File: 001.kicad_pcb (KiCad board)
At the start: 2 copper layers, 63.5 x 109.2 mm, 36 parts, among them CN11 02-XH-A, CN12 02-XH-A, CN21 02-XH-A, CN22 02-XH-A, J11 RJ45, J12 RJ45, J21 J21-FROM-PSE, J22 J22-PD-LAN, K11 JQC-3FF, K21 JQC-3FF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

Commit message: PCB変更とRJ45コネクタのFP作り
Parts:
- moved RV11 207.1 mm to (177.3, -757.9)
- moved FL11 205.2 mm to (196.6, -757.2)
- moved R11 140.2 mm to (169.7, -774.5)
- moved C11 92.1 mm to (64.1, -732.2)
- moved CN11 92.1 mm to (102.5, -742.4)
- moved D11 92.1 mm to (61.9, -749.5)
- moved D12 92.1 mm to (60.2, -726.0)
- moved D13 92.1 mm to (64.9, -716.0)
- moved F11 92.1 mm to (62.3, -740.7)
- moved R12 92.1 mm to (62.7, -711.5)
- moved U11 92.1 mm to (93.7, -714.2)
- moved CN12 92.1 mm to (96.1, -729.2)
- moved J12 51.4 mm to (217.9, -746.5), turned to 270 degrees
- moved J11 49.0 mm to (217.4, -770.6), turned to 270 degrees
- moved K11 20.7 mm to (200.4, -741.7), turned to 270 degrees

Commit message: もうちょっとRJ45コネクタは大変更
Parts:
- D23: value PWR LED -> LED
- J11, J12: footprint Connector_RJ:RJ45_Amphenol_RJHSE5380 -> HOLLY:RJ45_Neltron_7810-8P8C
- J21: value J21-FROM-PSE -> RJ45; footprint Connector_RJ:RJ45_Amphenol_RJHSE5380 -> HOLLY:RJ45_Neltron_7810-8P8C
- J22: value J22-PD-LAN -> RJ45; footprint Connector_RJ:RJ45_Amphenol_RJHSE5380 -> HOLLY:RJ45_Neltron_7810-8P8C
- moved J21 2.52 mm to (165.3, -817.6), turned to 270 degrees
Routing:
- net Net-(J22-Pad5): track 0.00 -> 30.5 mm
- net /PD1: track 30.5 -> 0.00 mm
- net /PD_PWR: track 39.9 -> 65.3 mm
- net /PD2: track 25.3 -> 0.00 mm

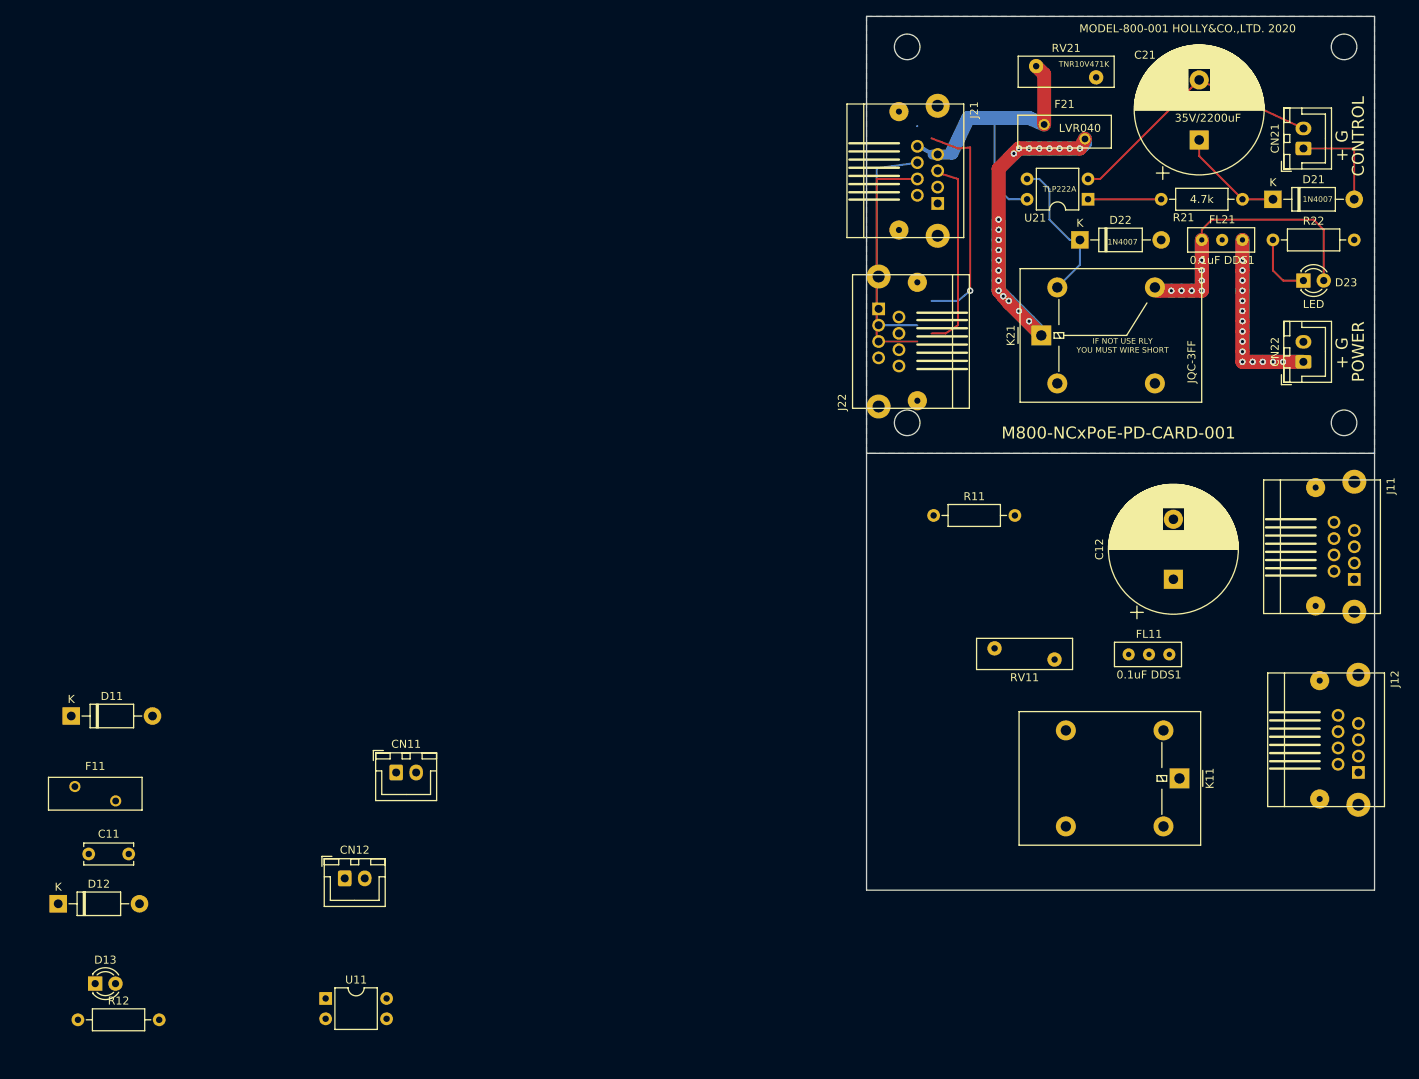
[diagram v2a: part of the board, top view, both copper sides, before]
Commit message: RJ45 SOCKETを組み直し
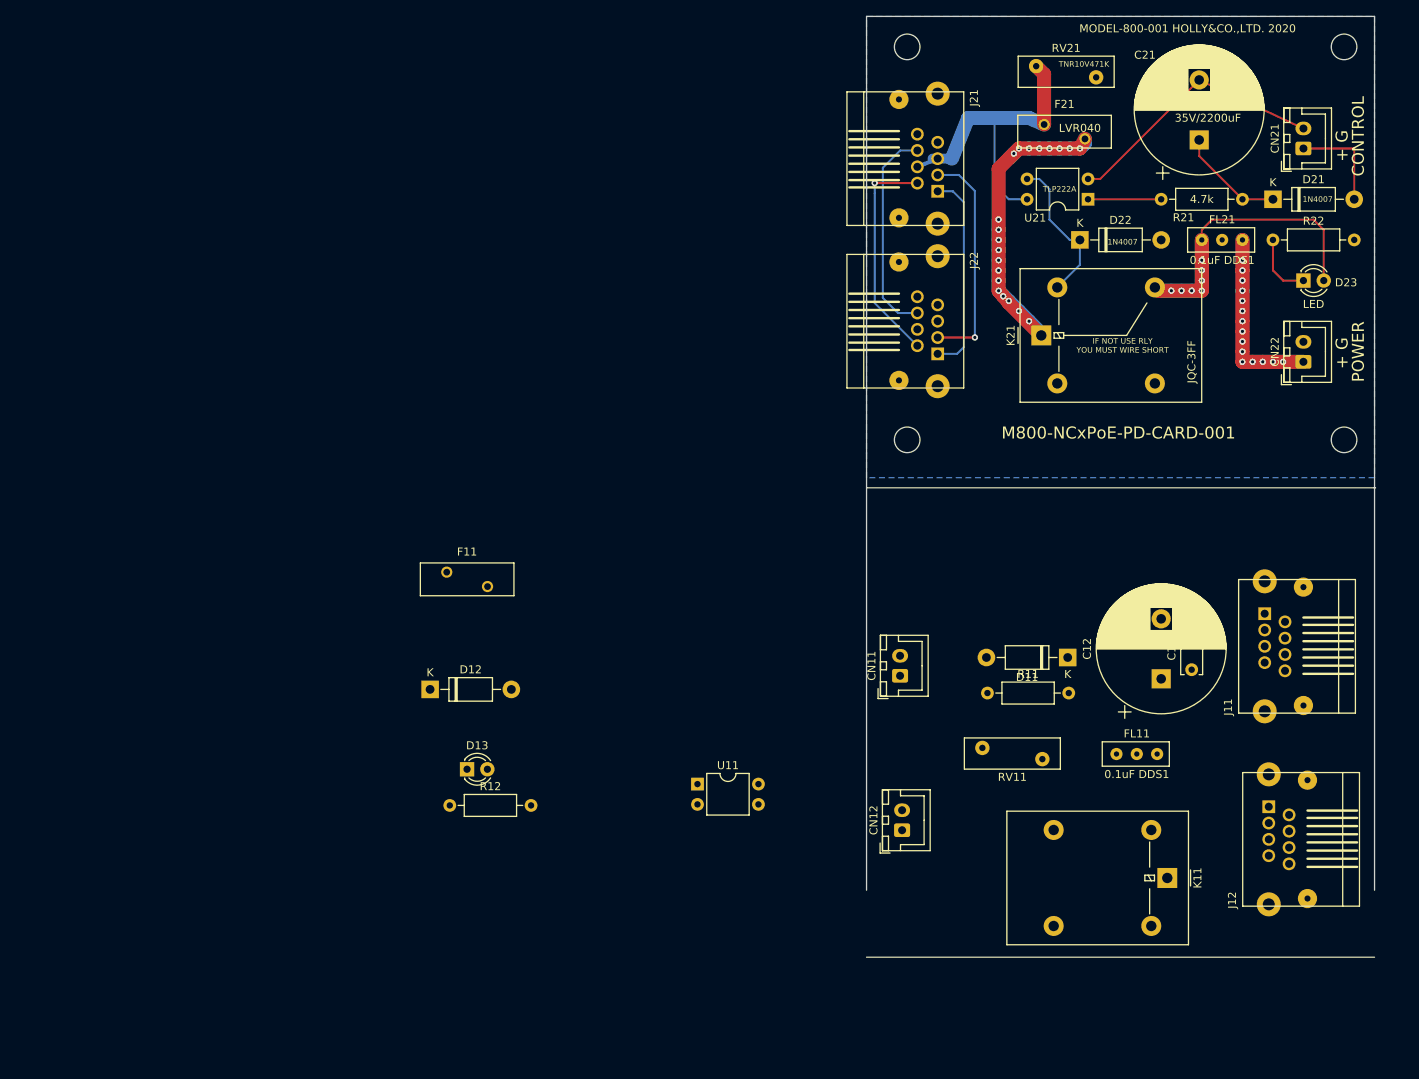
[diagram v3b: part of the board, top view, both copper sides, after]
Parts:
- moved C11 139.8 mm to (201.9, -755.3), turned to 90 degrees
- moved D11 124.8 mm to (186.4, -756.8), turned to 180 degrees
- moved CN12 69.9 mm to (165.7, -735.2), turned to 90 degrees
- moved CN11 64.1 mm to (165.5, -754.5), turned to 90 degrees
- moved F11 53.7 mm to (108.8, -767.5)
- moved D12 53.7 mm to (106.7, -752.8)
- moved D13 53.7 mm to (111.4, -742.8)
- moved U11 53.7 mm to (140.2, -741.0)
- moved R12 53.7 mm to (109.2, -738.3)
- moved R11 23.2 mm to (176.4, -752.3)
- moved C12 12.5 mm to (198.1, -754.1)
- moved FL11 12.5 mm to (195.1, -744.7)
- moved J12 12.5 mm to (216.4, -734.1), turned to 90 degrees
- moved RV11 12.5 mm to (175.8, -745.5)
- moved J11 12.5 mm to (215.9, -758.2), turned to 90 degrees
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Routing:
- net Net-(J22-Pad5): track 30.5 -> 0.00 mm
- net /PD2: track 0.00 -> 27.8 mm, vias 0 -> 1
- net /PD1: track 0.00 -> 25.6 mm
- net /PD_PWR: track 65.3 -> 40.7 mm
- net /PD4: track 28.3 -> 26.6 mm, vias 1 -> 0
- net /PD3: track 29.8 -> 28.4 mm, vias 0 -> 1
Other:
- board size 63.5 x 109.2 mm -> 63.6 x 117.6 mm

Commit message: 更に小型化
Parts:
- removed EC?: DSS1, M800-NCxPoE:DSS1
- removed the REF** at (221.0, -833.1)
- removed the REF** at (221.0, -784.0)
- removed the REF** at (166.4, -784.0)
- removed the REF** at (166.4, -833.1)
- added REF**: MountingHole_3.2mm_M3, MountingHole:MountingHole_3.2mm_M3, F.Cu at (229.9, 61.0)
- added REF**: MountingHole_3.2mm_M3, MountingHole:MountingHole_3.2mm_M3, F.Cu at (229.9, 110.5)
- added REF**: MountingHole_3.2mm_M3, MountingHole:MountingHole_3.2mm_M3, F.Cu at (181.6, 110.5)
- added REF**: MountingHole_3.2mm_M3, MountingHole:MountingHole_3.2mm_M3, F.Cu at (181.6, 61.0)
- moved FL21 905.6 mm to (219.7, 96.5), turned to 270 degrees
- moved D21 904.3 mm to (219.7, 90.2), turned to 90 degrees
- moved R21 904.2 mm to (212.1, 90.2), turned to 90 degrees
- moved D22 899.4 mm to (207.0, 90.2), turned to 90 degrees
- moved D23 899.2 mm to (226.1, 95.2)
- moved CN22 899.2 mm to (219.7, 105.4), turned to 0 degrees
- moved K21 898.7 mm to (195.6, 101.6)
- moved CN21 895.4 mm to (227.3, 74.9)
- moved J22 894.2 mm to (180.6, 95.2)
- moved J21 894.2 mm to (180.6, 74.9)
- moved F21 894.2 mm to (195.6, 70.7)
- moved RV21 894.2 mm to (201.9, 64.8)
- moved C21 894.2 mm to (214.6, 72.6)
- moved U21 894.2 mm to (200.7, 80.0), turned to 270 degrees
- moved R22 889.1 mm to (226.1, 80.0), turned to 270 degrees
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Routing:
- net Net-(CN22-Pad1): track 45.7 -> 6.35 mm, vias 15 -> 0
- net /PD_PWR: track 40.7 -> 69.2 mm, vias 0 -> 11
- net Net-(C21-Pad2): track 33.4 -> 47.4 mm
- net Net-(D23-Pad2): track 48.7 -> 36.4 mm, vias 7 -> 5
- net Net-(C21-Pad1): track 13.5 -> 25.2 mm
- net Net-(D23-Pad1): track 8.15 -> 17.9 mm
- net Net-(F21-Pad2): track 63.1 -> 72.5 mm, vias 20 -> 29
- net Net-(R21-Pad2): track 9.14 -> 15.0 mm
- net /PD1: track 25.6 -> 24.3 mm
- net /PD3: track 28.4 -> 27.3 mm
- net Net-(CN21-Pad1): track 12.7 -> 12.0 mm
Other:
- board size 63.6 x 117.6 mm -> 162.6 x 57.2 mm

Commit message: 一応完成、これからガーバー
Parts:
- added REF**: MountingHole_3.2mm_M3, MountingHole:MountingHole_3.2mm_M3, F.Cu at (122.1, 111.8)
- added REF**: MountingHole_3.2mm_M3, MountingHole:MountingHole_3.2mm_M3, F.Cu at (73.8, 111.8)
- added REF**: MountingHole_3.2mm_M3, MountingHole:MountingHole_3.2mm_M3, F.Cu at (73.8, 63.8)
- added REF**: MountingHole_3.2mm_M3, MountingHole:MountingHole_3.2mm_M3, F.Cu at (122.1, 63.8)
- moved R12 35.9 mm to (76.2, 83.2), turned to 270 degrees
- moved F11 34.4 mm to (106.0, 78.1), turned to 180 degrees
- moved U11 27.1 mm to (106.0, 83.2), turned to 270 degrees
- moved D12 26.8 mm to (99.7, 92.7), turned to 90 degrees
- moved RV11 26.8 mm to (108.0, 71.1), turned to 180 degrees
- moved FL11 25.0 mm to (83.8, 99.7), turned to 90 degrees
- moved D11 23.1 mm to (81.3, 92.7), turned to 90 degrees
- moved C12 21.2 mm to (88.3, 75.6)
- moved C11 17.4 mm to (101.6, 64.8), turned to 180 degrees
- moved D13 14.5 mm to (73.7, 99.1)
- moved CN12 13.3 mm to (83.8, 109.2), turned to 180 degrees
- moved J11 10.3 mm to (121.3, 77.5)
- moved J12 9.86 mm to (121.3, 97.8)
- moved R11 9.16 mm to (95.9, 84.5), turned to 180 degrees
- moved K21 2.79 mm to (192.8, 101.6)
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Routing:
- net /PSE_PWR: track 0.00 -> 83.6 mm
- net Net-(C11-Pad2): track 0.00 -> 54.3 mm
- net Net-(F11-Pad2): track 0.00 -> 46.8 mm
- net Net-(C11-Pad1): track 0.00 -> 38.2 mm
- net Net-(F11-Pad1): track 0.00 -> 30.7 mm
- net /PSEBUS2: track 0.00 -> 26.9 mm
- net /PSEBUS4: track 0.00 -> 24.4 mm
- net /PSEBUS1: track 0.00 -> 23.1 mm
- net /PSEBUS3: track 0.00 -> 23.1 mm
- net Net-(D12-Pad1): track 0.00 -> 17.1 mm
- net Net-(R11-Pad1): track 0.00 -> 13.4 mm
- net Net-(CN22-Pad1): track 6.35 -> 16.3 mm
- net Net-(CN11-Pad1): track 0.00 -> 7.82 mm
- net Net-(CN12-Pad1): track 0.00 -> 6.98 mm
- net /PSE_GND: track 0.00 -> 6.66 mm, vias 0 -> 2
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- added copper zone on B.Cu, net /PSE_GND
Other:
- board size 162.6 x 57.2 mm -> 162.4 x 58.7 mm
- board text added: "G +"
- board text added: "M800-NCxPoE-PSE-CARD-001"

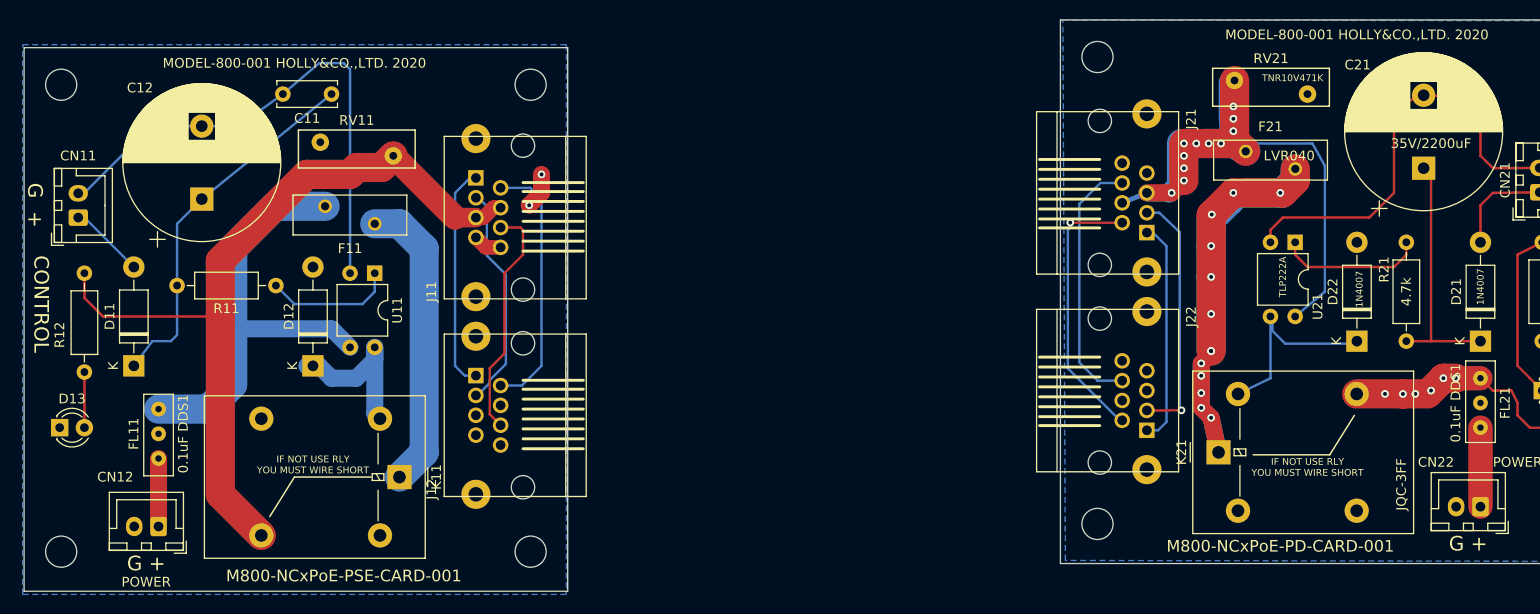
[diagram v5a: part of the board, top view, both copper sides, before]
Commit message: PSEとPDを別図面にした
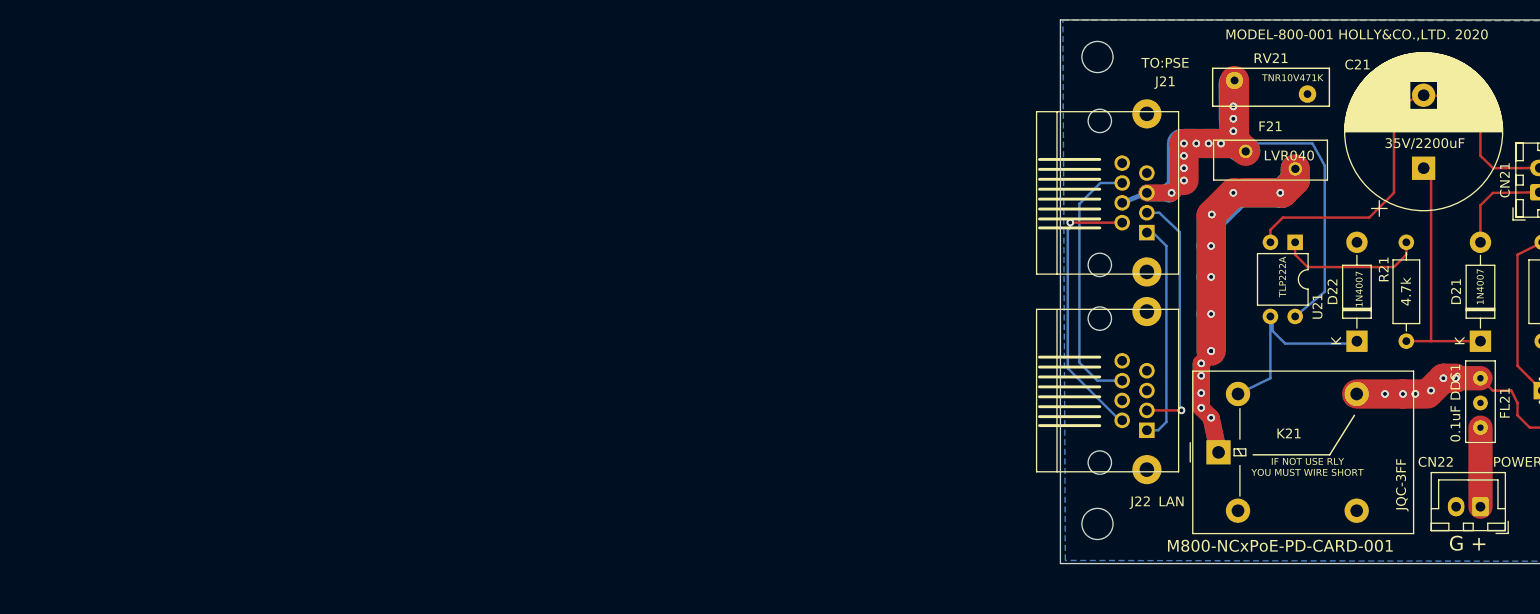
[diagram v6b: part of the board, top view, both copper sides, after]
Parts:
- removed C11: 35V/10uF, Capacitor_THT:C_Disc_D6.0mm_W2.5mm_P5.00mm
- removed C12: 35V/2200uF, Capacitor_THT:CP_Radial_D16.0mm_P7.50mm
- removed CN11, CN12: 02-XH-A, Connector_JST:JST_XH_B2B-XH-A_1x02_P2.50mm_Vertical
- removed D11, D12: 1N4007, Diode_THT:D_DO-41_SOD81_P10.16mm_Horizontal
- removed D13: LED, LED_THT:LED_D3.0mm
- removed F11: LVR040, Fuse:Fuse_BelFuse_0ZRE0033FF_L11.4mm_W3.8mm
- removed FL11: 0.1uF DDS1, HOLLY:DSS1
- removed J11, J12: RJ45, HOLLY:RJ45_Neltron_7810-8P8C
- removed K11: JQC-3FF, Relay_THT:Relay_SPDT_Omron-G5LE-1
- removed R11: 4.7k, Resistor_THT:R_Axial_DIN0207_L6.3mm_D2.5mm_P10.16mm_Horizontal
- removed R12: R_US, Resistor_THT:R_Axial_DIN0207_L6.3mm_D2.5mm_P10.16mm_Horizontal
- removed the REF** at (122.1, 111.8)
- removed the REF** at (73.8, 111.8)
- removed the REF** at (73.8, 63.8)
- removed the REF** at (122.1, 63.8)
- removed RV11: TNR10V471K, Varistor:RV_Disc_D12mm_W3.9mm_P7.5mm
- removed U11: TLP222A, Package_DIP:DIP-4_W7.62mm
- added ?: , , F.Cu at (-13.3, -2.54)
- added ?: , , F.Cu at (22.9, -6.99)
- added ? (x2): , , F.Cu at (85.1, 73.0)
- added ?: , , F.Cu at (87.0, 73.0)
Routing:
- net /PSE_PWR: track 83.6 -> 0.00 mm
- net Net-(C11-Pad2): track 54.3 -> 0.00 mm
- net Net-(F11-Pad2): track 46.8 -> 0.00 mm
- net Net-(C11-Pad1): track 38.2 -> 0.00 mm
- net Net-(F11-Pad1): track 30.7 -> 0.00 mm
- net /PSEBUS2: track 26.9 -> 0.00 mm
- net /PSEBUS4: track 24.4 -> 0.00 mm
- net /PSEBUS1: track 23.1 -> 0.00 mm
- net /PSEBUS3: track 23.1 -> 0.00 mm
- net Net-(D12-Pad1): track 17.1 -> 0.00 mm
- net Net-(R11-Pad1): track 13.4 -> 0.00 mm
- net Net-(CN11-Pad1): track 7.82 -> 0.00 mm
- net Net-(CN12-Pad1): track 6.98 -> 0.00 mm
- net /PSE_GND: track 6.66 -> 0.00 mm, vias 2 -> 0
- net Net-(D13-Pad2): track 5.72 -> 0.00 mm
- removed copper zone on B.Cu, net /PSE_GND
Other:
- board size 162.4 x 58.7 mm -> 55.9 x 55.9 mm
- board text added: "LAN"
- board text added: "TO:PSE"
- board text removed: "M800-NCxPoE-PSE-CARD-001"

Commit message: version合わせ
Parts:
- removed the ? at (85.1, 73.0) (x2)
- added ? (x2): , , F.Cu at (85.1, 73.0)
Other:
- net class Default removed
